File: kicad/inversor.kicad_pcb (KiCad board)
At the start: 2 copper layers, 178 x 76 mm, 87 parts, among them J1 VCC, J10 To IGBTs, J2 PWM, J3 LCD 16x2, J4 MainFan, J5 380VFreed, J6 PRO_MINI_L, J8 PRO_MINI_R, J9 SPWM Driver Board, Q1 SSF6014D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

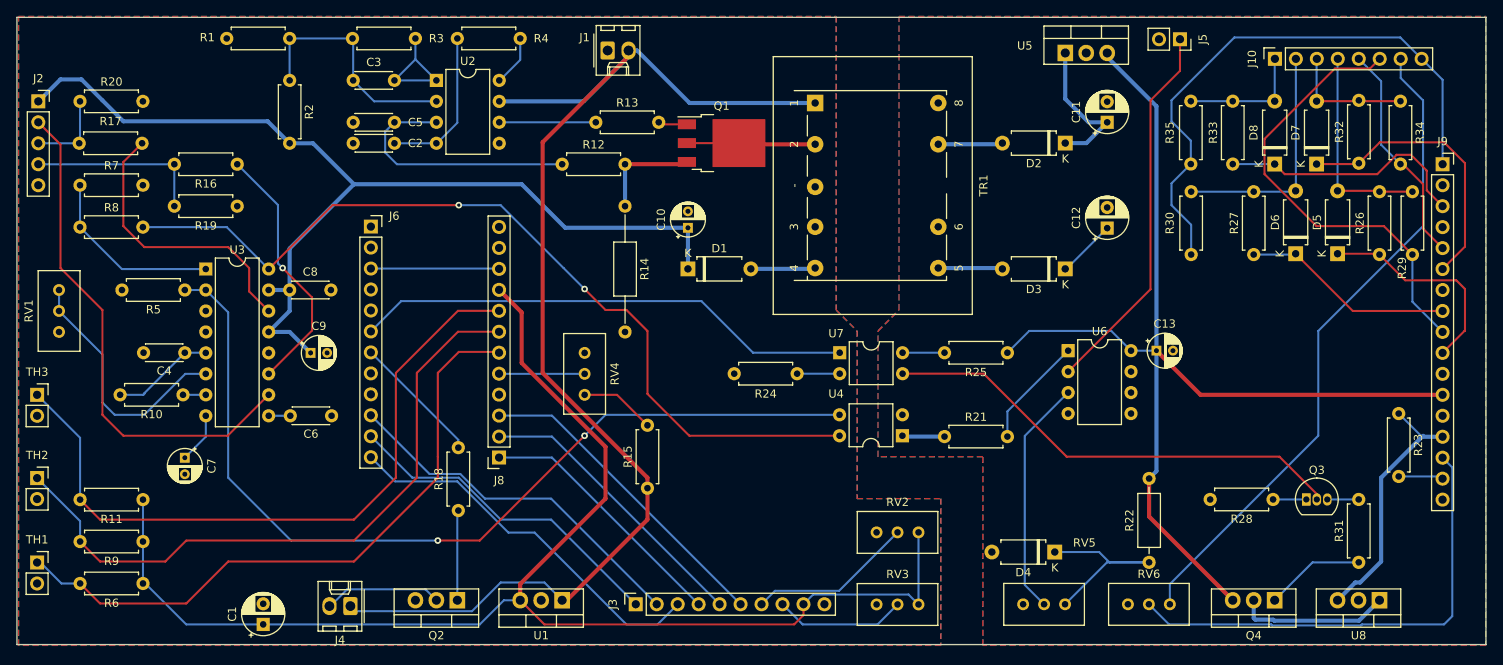
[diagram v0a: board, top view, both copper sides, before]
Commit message: Fix: - Agregado condensador en la linea VCC - Agregada línea entre D13 del arduino y DS del SG3525 para poder detenerlo - Ajustes en pistas
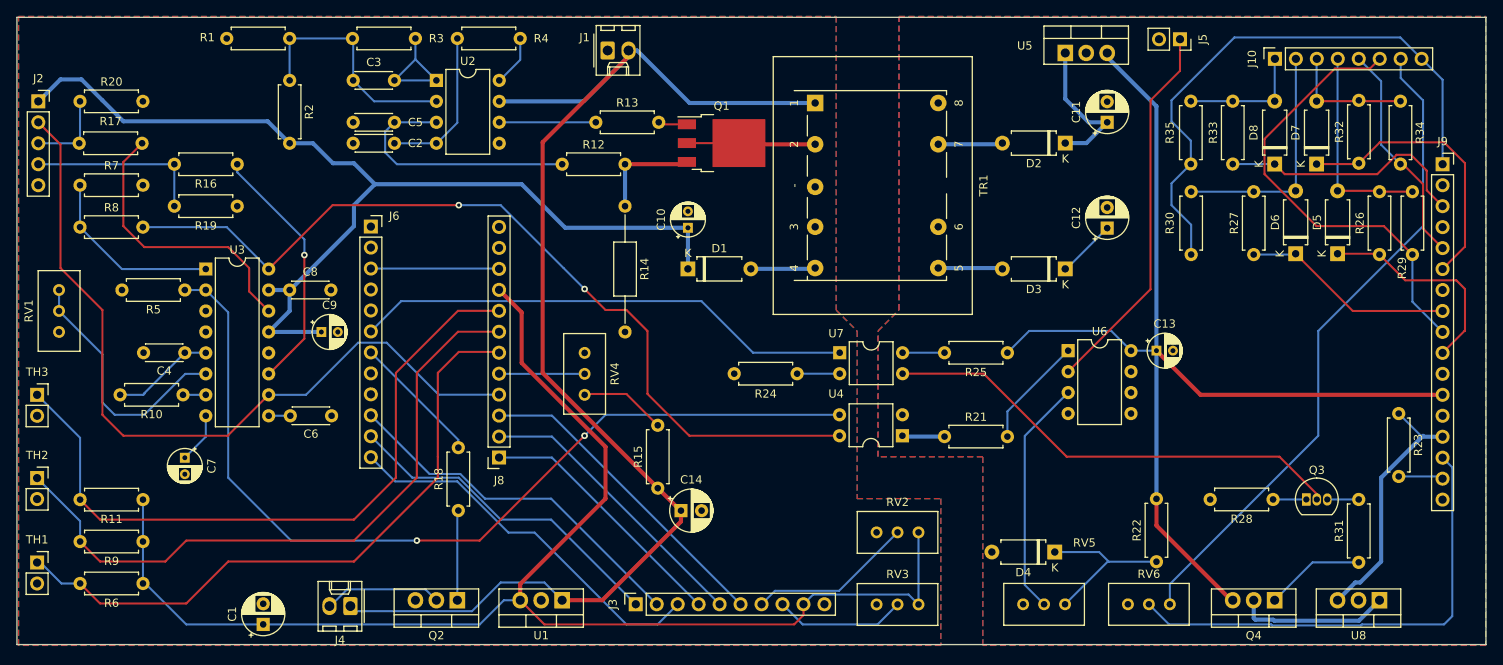
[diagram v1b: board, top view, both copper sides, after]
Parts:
- added C14: 250nF, Capacitor_THT:CP_Radial_D5.0mm_P2.50mm, F.Cu at (156.5, 85.3)
- R22: footprint Resistor_THT:R_Axial_DIN0207_L6.3mm_D2.5mm_P10.16mm_Horizontal -> Resistor_THT:R_Axial_DIN0207_L6.3mm_D2.5mm_P7.62mm_Horizontal
- moved C9 2.85 mm to (112.9, 63.6)
- moved R15 1.25 mm to (153.7, 82.5)
- moved R22 0.89 mm to (214.1, 91.5)
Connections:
- J2 pad 2: SD -> D13
- U3 pad 10: SD -> D13
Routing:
- net D13: track 0.00 -> 95.0 mm
- net SD: track 61.9 -> 0.00 mm
- net VCC: track 152.9 -> 158.8 mm
- net Net-(D4-Pad1): track 24.2 -> 20.1 mm
- net +15V: track 122.9 -> 124.2 mm
- net Net-(R15-Pad2): track 9.14 -> 10.4 mm
- net Net-(R16-Pad1): track 31.3 -> 30.4 mm
- net +12V: track 130.4 -> 129.8 mm
